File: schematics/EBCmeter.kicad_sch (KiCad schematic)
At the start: 54 parts, among them J1 BlueSense, J2 BlueLink, J3 RedLink, Q1 BSS214NH, Q2 BSS214NH, Q3 BSS214NH, Q4 BSS214NH, U1 TSZ121ILT, U2 LP5907MFX-3.3, U3 MCP3550-50-EMS, U4 TSZ121IDT, U5 LM4040, U6 REF3033, U7 DG9431EDY-T1-GE3, U8 REF3012, U9 REF3033

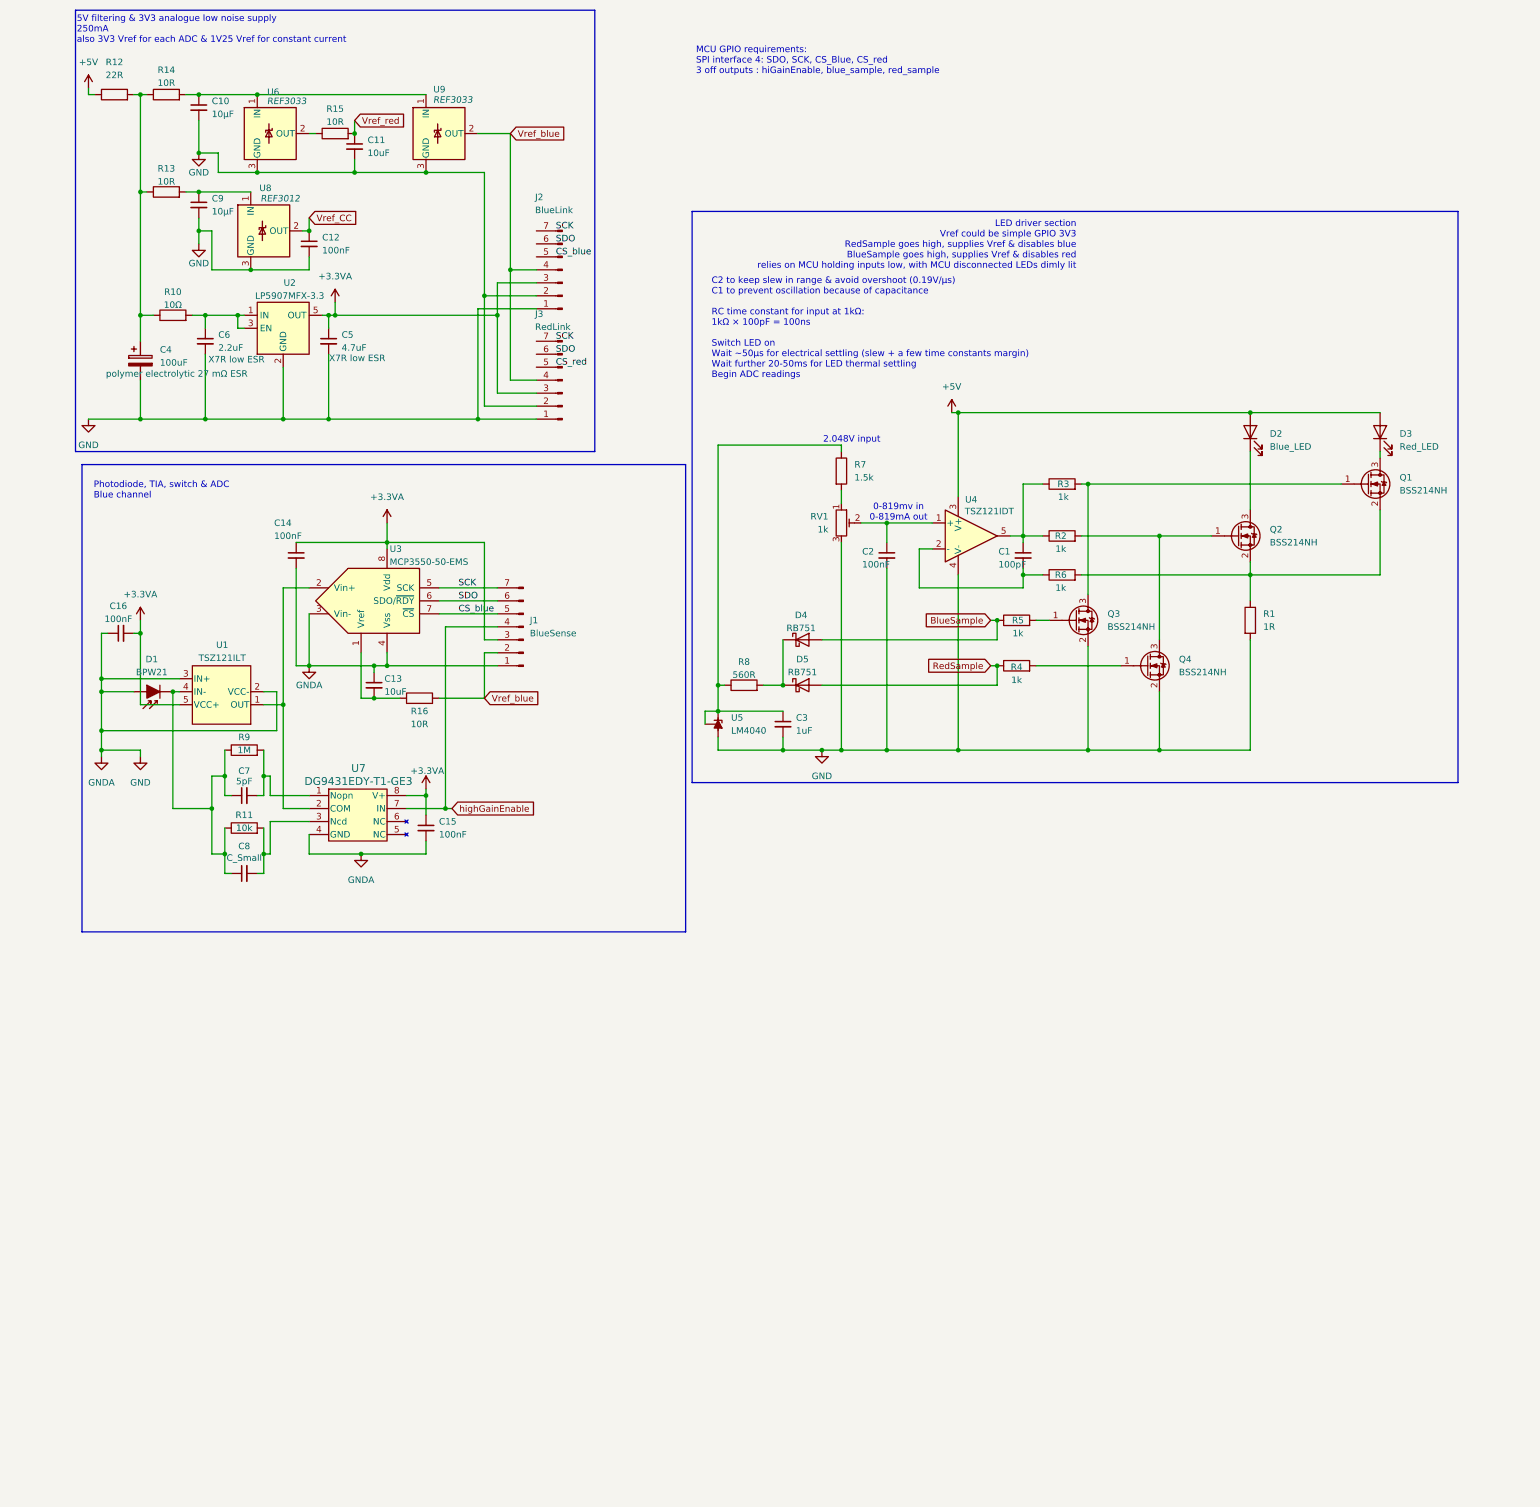
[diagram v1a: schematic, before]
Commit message: refinement, additional schematics
work in progress

MCU controls peripherals - LED constant current, ADC & analogue SPDT switch

envisage 1 digital board with MCU, LED control, LDO's & filtering
2 separate analogue boards with photodiode, ADC & analogue switch

PCB layout TBD
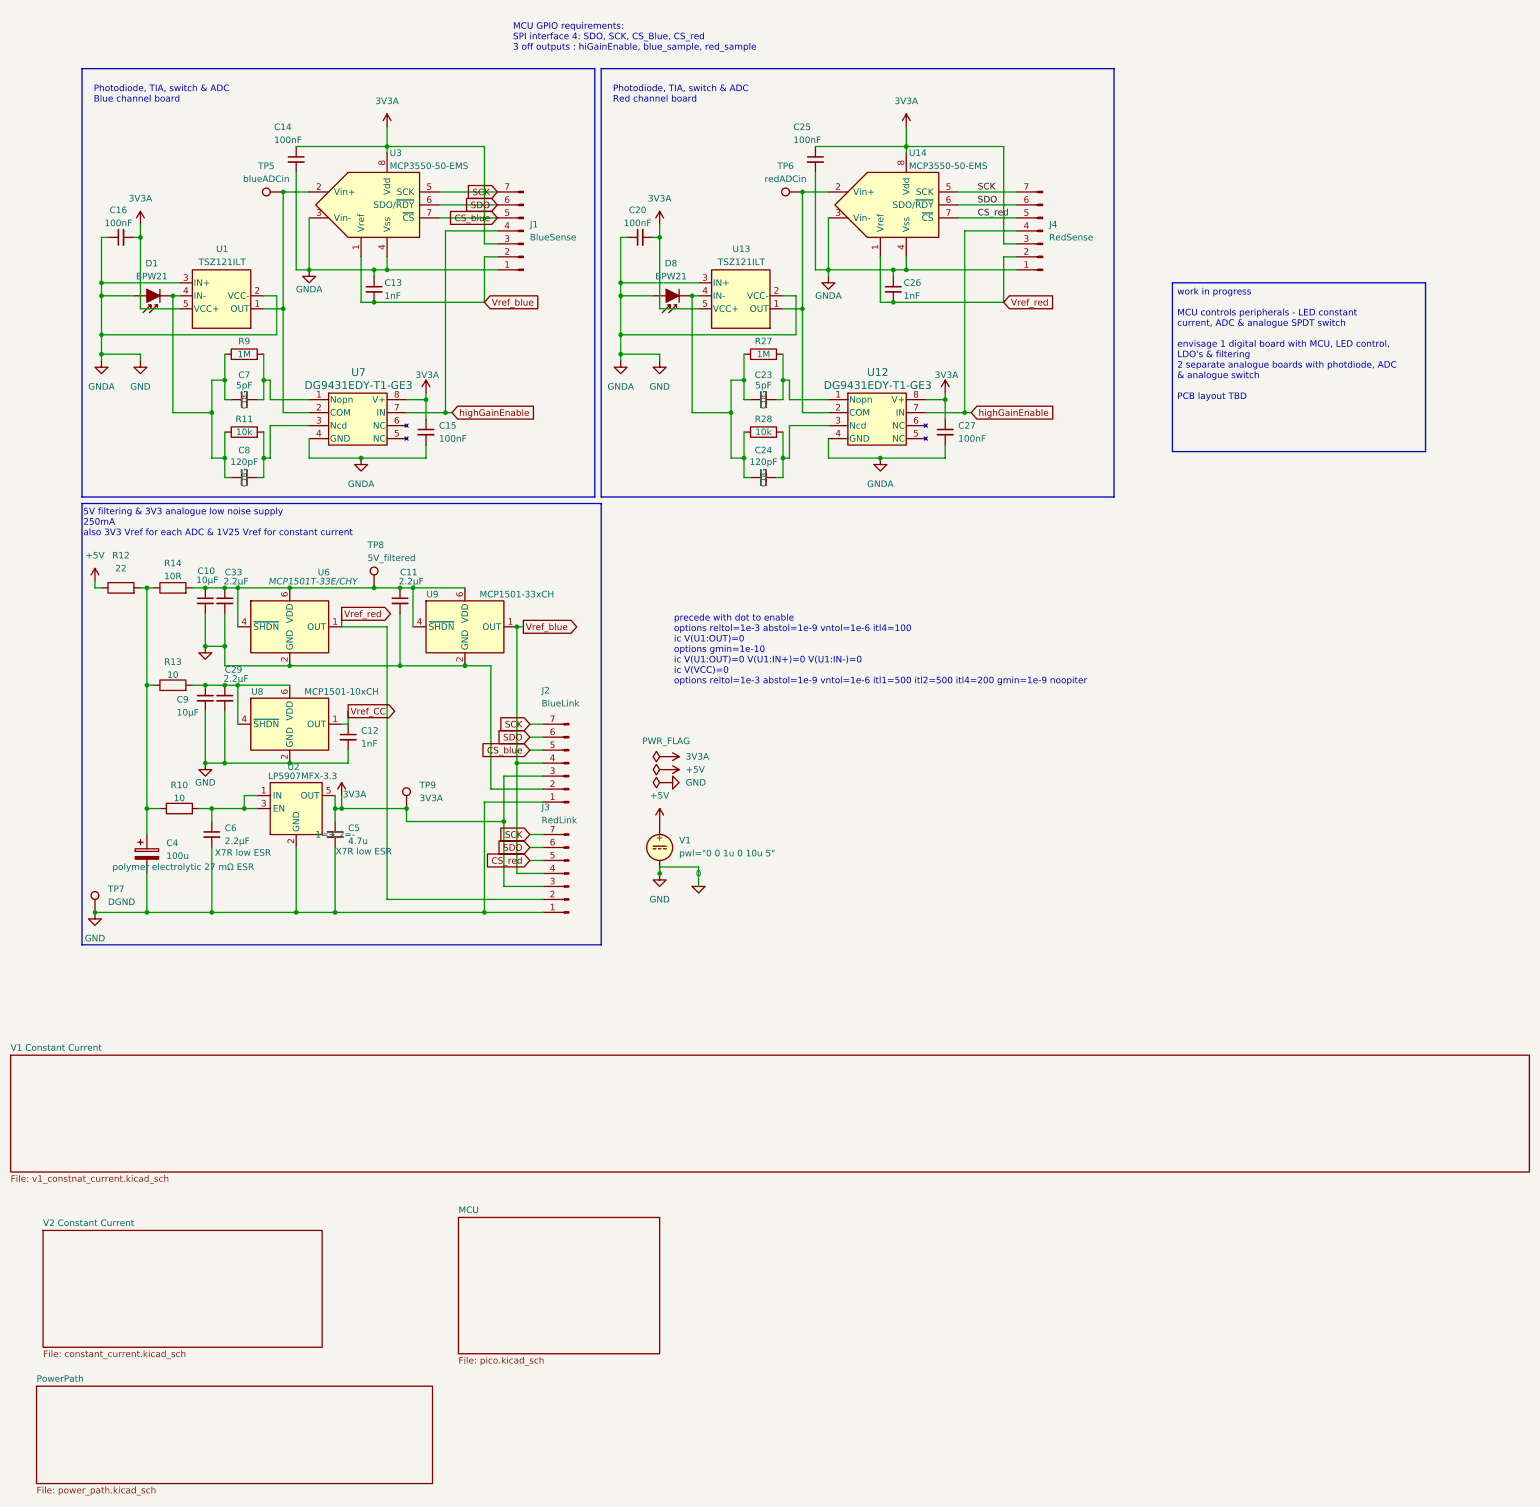
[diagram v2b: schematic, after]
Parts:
- removed C1: 100pF, symbol Device:C_Small
- removed C2: 100nF, symbol Device:C_Small
- removed C3: 1uF, symbol Device:C_Small
- removed D2: Blue_LED, symbol Device:LED
- removed D3: Red_LED, symbol Device:LED
- removed D4, D5: RB751, Diode_SMD:D_SOD-323F, symbol Diode:BAT54J
- removed Q1, Q2, Q3, Q4: BSS214NH, Package_TO_SOT_SMD:SOT-323_SC-70, symbol Transistor_FET:BSS214NW
- removed R1: 1R, symbol Device:R
- removed R15, R16: 10R, symbol Device:R
- removed R2, R3, R4, R5, R6: 1k, symbol Device:R
- removed R7: 1.5k, symbol Device:R
- removed R8: 560R, symbol Device:R
- removed RV1: 1k, Potentiometer_THT:Potentiometer_Bourns_3296W_Vertical, symbol Device:R_Potentiometer_Trim
- removed U4: TSZ121IDT, symbol Simulation_SPICE:OPAMP
- removed U5: LM4040, Package_TO_SOT_SMD:SOT-23, symbol Reference_Voltage:TL431DBZ
- added C20, C25, C27: 100nF, Capacitor_SMD:C_0805_2012Metric_Pad1.18x1.45mm_HandSolder, symbol Device:C_Small
- added C23: 5pF, Capacitor_SMD:C_0603_1608Metric, symbol Device:C_Small
- added C24: 120pF, Capacitor_SMD:C_0603_1608Metric, symbol Device:C_Small
- added C26: 1nF, Capacitor_SMD:C_0805_2012Metric_Pad1.18x1.45mm_HandSolder, symbol Device:C_Small
- added C29, C33: 2.2µF, Capacitor_SMD:C_0805_2012Metric_Pad1.18x1.45mm_HandSolder, symbol Device:C_Small
- added D8: BPW21, Package_TO_SOT_THT:TO-39-2_Window, symbol Device:D_Photo_Filled
- added J4: RedSense, Connector_PinHeader_2.54mm:PinHeader_1x07_P2.54mm_Vertical, symbol Connector:Conn_01x07_Pin
- added R27: 1M, Resistor_SMD:R_0603_1608Metric, symbol Device:R
- added R28: 10k, Capacitor_SMD:C_0603_1608Metric, symbol Device:R
- added TP5: blueADCin, Connector_PinHeader_2.54mm:PinHeader_1x01_P2.54mm_Vertical, symbol Connector:TestPoint
- added TP6: redADCin, Connector_PinHeader_2.54mm:PinHeader_1x01_P2.54mm_Vertical, symbol Connector:TestPoint
- added TP7: DGND, Connector_PinHeader_2.54mm:PinHeader_1x01_P2.54mm_Vertical, symbol Connector:TestPoint
- added TP8: 5V_filtered, Connector_PinHeader_2.54mm:PinHeader_1x01_P2.54mm_Vertical, symbol Connector:TestPoint
- added TP9: 3V3A, Connector_PinHeader_2.54mm:PinHeader_1x01_P2.54mm_Vertical, symbol Connector:TestPoint
- added U12: DG9431EDY-T1-GE3, Personal_Library:SOIC_DG9431EDY-T1-GE3_VIS, symbol Personal_Library:DG9431EDY-T1-GE3
- added U13: TSZ121ILT, Personal_Library:SOT23-5_STM, symbol Personal_Library:TSZ121ILT
- added U14: MCP3550-50-EMS, Personal_Library:SOIC8-N_MC_MCH, symbol Analog_ADC:MCP3550-50-EMS
- added V1: ${SIM.PARAMS}, symbol Simulation_SPICE:VDC
- C10, C14, C15, C16, C9: footprint (none) -> Capacitor_SMD:C_0805_2012Metric_Pad1.18x1.45mm_HandSolder
- C11: value 10uF -> 2.2µF; footprint (none) -> Capacitor_SMD:C_0805_2012Metric_Pad1.18x1.45mm_HandSolder
- C12: value 100nF -> 1nF; footprint (none) -> Capacitor_SMD:C_0805_2012Metric_Pad1.18x1.45mm_HandSolder
- C13: value 10uF -> 1nF; footprint (none) -> Capacitor_SMD:C_0805_2012Metric_Pad1.18x1.45mm_HandSolder
- C4: value 100uF -> 100u; footprint (none) -> Capacitor_SMD:C_Elec_6.3x5.8
- C5: value 4.7uF -> 4.7u; footprint (none) -> Capacitor_SMD:C_0805_2012Metric_Pad1.18x1.45mm_HandSolder
- C6: value 2.2uF -> 2.2µF; footprint (none) -> Capacitor_SMD:C_0805_2012Metric_Pad1.18x1.45mm_HandSolder
- C7, R11: footprint (none) -> Capacitor_SMD:C_0603_1608Metric
- C8: value C_Small -> 120pF; footprint (none) -> Capacitor_SMD:C_0603_1608Metric
- J1, J2, J3: footprint (none) -> Connector_PinHeader_2.54mm:PinHeader_1x07_P2.54mm_Vertical
- R10: value 10Ω -> 10; footprint (none) -> Resistor_SMD:R_0805_2012Metric_Pad1.20x1.40mm_HandSolder
- R12: value 22R -> 22; footprint (none) -> Resistor_SMD:R_0805_2012Metric_Pad1.20x1.40mm_HandSolder
- R13: value 10R -> 10; footprint (none) -> Resistor_SMD:R_0805_2012Metric_Pad1.20x1.40mm_HandSolder
- R14: footprint (none) -> Resistor_SMD:R_0805_2012Metric_Pad1.20x1.40mm_HandSolder
- R9: footprint (none) -> Resistor_SMD:R_0603_1608Metric
- U1: footprint SOT23-5_STM -> Personal_Library:SOT23-5_STM
- U3: footprint (none) -> Personal_Library:SOIC8-N_MC_MCH
- U6: value REF3033 -> MCP1501T-33E/CHY; footprint Package_TO_SOT_SMD:SOT-23 -> Package_TO_SOT_SMD:SOT-23-6; symbol Reference_Voltage:REF3033 -> Reference_Voltage:MCP1501-33xCH
- U7: footprint SOIC_DG9431EDY-T1-GE3_VIS -> Personal_Library:SOIC_DG9431EDY-T1-GE3_VIS
- U8: value REF3012 -> MCP1501-10xCH; footprint Package_TO_SOT_SMD:SOT-23 -> Package_TO_SOT_SMD:SOT-23-6; symbol Reference_Voltage:REF3012 -> Reference_Voltage:MCP1501-10xCH
- U9: value REF3033 -> MCP1501-33xCH; footprint Package_TO_SOT_SMD:SOT-23 -> Package_TO_SOT_SMD:SOT-23-6; symbol Reference_Voltage:REF3033 -> Reference_Voltage:MCP1501-33xCH
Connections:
- net +5V: now also V1.1
- net CS_blue: now also J2.5 (Pin_5)
- net CS_red: now also J3.5 (Pin_5), J4.5 (Pin_5), U14.7 (~{CS})
- net SCK: now also J2.7 (Pin_7), J3.7 (Pin_7), J4.7 (Pin_7), U14.5 (SCK)
- net SDO: now also J2.6 (Pin_6), J3.6 (Pin_6), J4.6 (Pin_6), U14.6 (SDO/~{RDY})
- net Vref_CC: now also U8.1 (OUT); no longer U8.2 (OUT)
- net Vref_blue: now also C13.2, U3.1 (Vref), U9.1 (OUT); no longer U9.2 (OUT)
- net Vref_red: now also J3.2 (Pin_2), U6.1 (OUT), C26.2, J4.2 (Pin_2), U14.1 (Vref); no longer C11.1
- net highGainEnable: now also J4.4 (Pin_4), U12.7 (IN)
- net at C10.1, R14.2: now also C11.1, U6.4 (~{SHDN}), U6.6 (VDD), U9.4 (~{SHDN}), U9.6 (VDD), C33.1, TP8.1; no longer U6.1 (IN), U9.1 (IN)
- net at U1.1 (OUT), U3.2 (Vin+), U7.2 (COM): now also TP5.1
- net 0: now reaches U6.2 (GND)
- net 0: now also C10.2, C11.2, C12.2, C13.1, C14.2, C15.2, C16.1, C4.2, C5.2, C6.2, C9.2, D1.2 (A), J1.1 (Pin_1), J2.1 (Pin_1), J2.2 (Pin_2), J3.1 (Pin_1), U1.2 (VCC-), U1.3 (IN+), U2.2 (GND), U3.3 (Vin-), U3.4 (Vss), U6.3 (GND), U6.5 (GND), U7.4 (GND), U8.2 (GND), U8.3 (GND), U8.5 (GND), U9.2 (GND), U9.3 (GND), U9.5 (GND), C20.1, C25.2, C26.1, C27.2, C29.2, C33.2, D8.2 (A), J4.1 (Pin_1), TP7.1, U12.4 (GND), U13.2 (VCC-), U13.3 (IN+), U14.3 (Vin-), U14.4 (Vss), V1.2
- net at C9.1, R13.2: now also U8.4 (~{SHDN}), U8.6 (VDD), C29.1; no longer U8.1 (IN)
- net +3.3VA renamed 3V3A
- net 3V3A: now also C20.2, C25.1, C27.1, J4.3 (Pin_3), TP9.1, U12.8 (V+), U13.5 (VCC+), U14.8 (Vdd)
- removed net GND: C10.2, C11.2, C12.2, C13.1, C14.2, C15.2, C16.1, C4.2, C5.2, C6.2, C9.2, D1.2 (A), J1.1 (Pin_1), J2.1 (Pin_1), J2.2 (Pin_2), J3.1 (Pin_1), J3.2 (Pin_2), U1.2 (VCC-), U1.3 (IN+), U2.2 (GND), U3.3 (Vin-), U3.4 (Vss), U6.3 (GND), U7.4 (GND), U8.3 (GND), U9.3 (GND)
- new net: TP6.1, U12.2 (COM), U13.1 (OUT), U14.2 (Vin+)
- new net: C23.1, C24.1, D8.1 (K), R27.1, R28.1, U13.4 (IN-)
- new net: C23.2, R27.2, U12.1 (Nopn)
- new net: C24.2, R28.2, U12.3 (Ncd)
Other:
- added sheet MCU (pico.kicad_sch)
- added sheet PowerPath (power_path.kicad_sch)
- added sheet V1 Constant Current (v1_constnat_current.kicad_sch)
- added sheet V2 Constant Current (constant_current.kicad_sch)
- note added: "Photodiode, TIA, switch & ADC Blue channel board"
- note added: "Photodiode, TIA, switch & ADC Red channel board"
- note added: "precede with dot to enable options reltol=1e-3 abstol=1e-9 vntol=1e-6 itl4=100 ic V(U1:OUT)=0 options gmin=1e-10 ic V(U1:OUT)=0 V(U1:IN+)=0 V(U1:IN-)=0 ic V(VCC)=0 options reltol=1e-3 abstol=1e-9 vntol=1e-6 itl1=500 itl2=500 itl4=200 gmin=1e-9 noopiter"
- note removed: "0-819mv in 0-819mA out"
- note removed: "2.048V input"
- note removed: "C2 to keep slew in range & avoid overshoot (0.19V/µs) C1 to prevent oscillation because of capacitance RC time constant for input at 1kΩ: 1kΩ × 100pF = 100ns Switch LED on Wait ~50µs for electrical settling (slew + a few time constants margin) Wait further 20-50ms for LED thermal settling Begin ADC readings"
- note removed: "LED driver section Vref could be simple GPIO 3V3 RedSample goes high, supplies Vref & disables blue BlueSample goes high, supplies Vref & disables red relies on MCU holding inputs low, with MCU disconnected LEDs dimly lit"
- note removed: "Photodiode, TIA, switch & ADC Blue channel"
- moved on the sheet: C10, C12, C13, C14, C15, C16, C4, C5, C6, C7, C8, C9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
